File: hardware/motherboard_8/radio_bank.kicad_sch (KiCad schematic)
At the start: 7 parts, among them J1 RADIO 1-4, J2 RADIO 5-8, U2 AMS1117-3.3

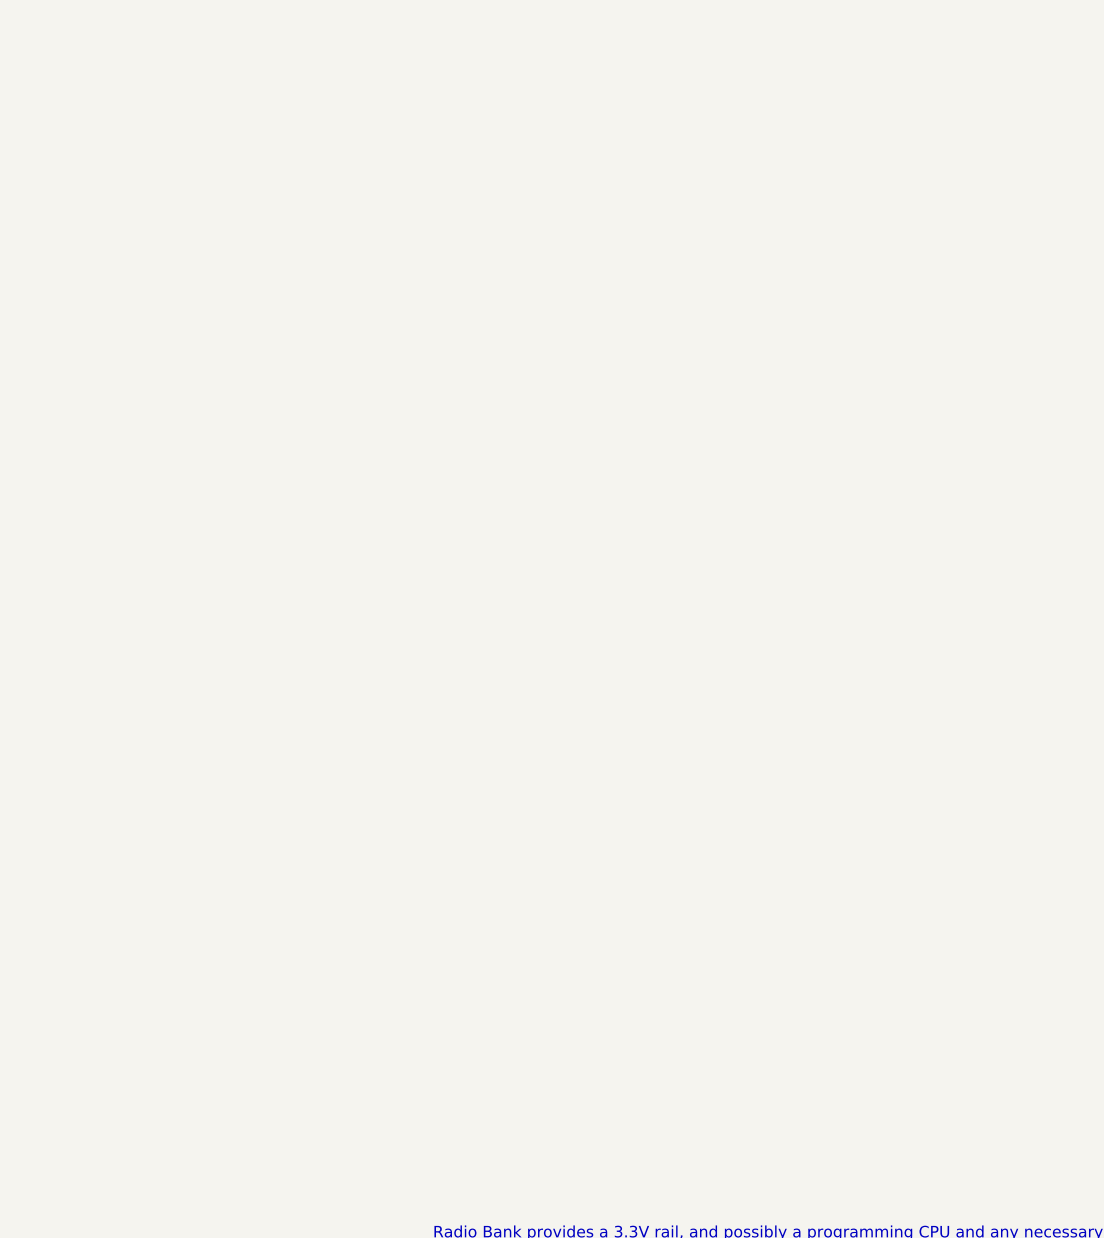
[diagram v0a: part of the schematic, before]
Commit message: Create motherboard 8. Now upgrade number of radios
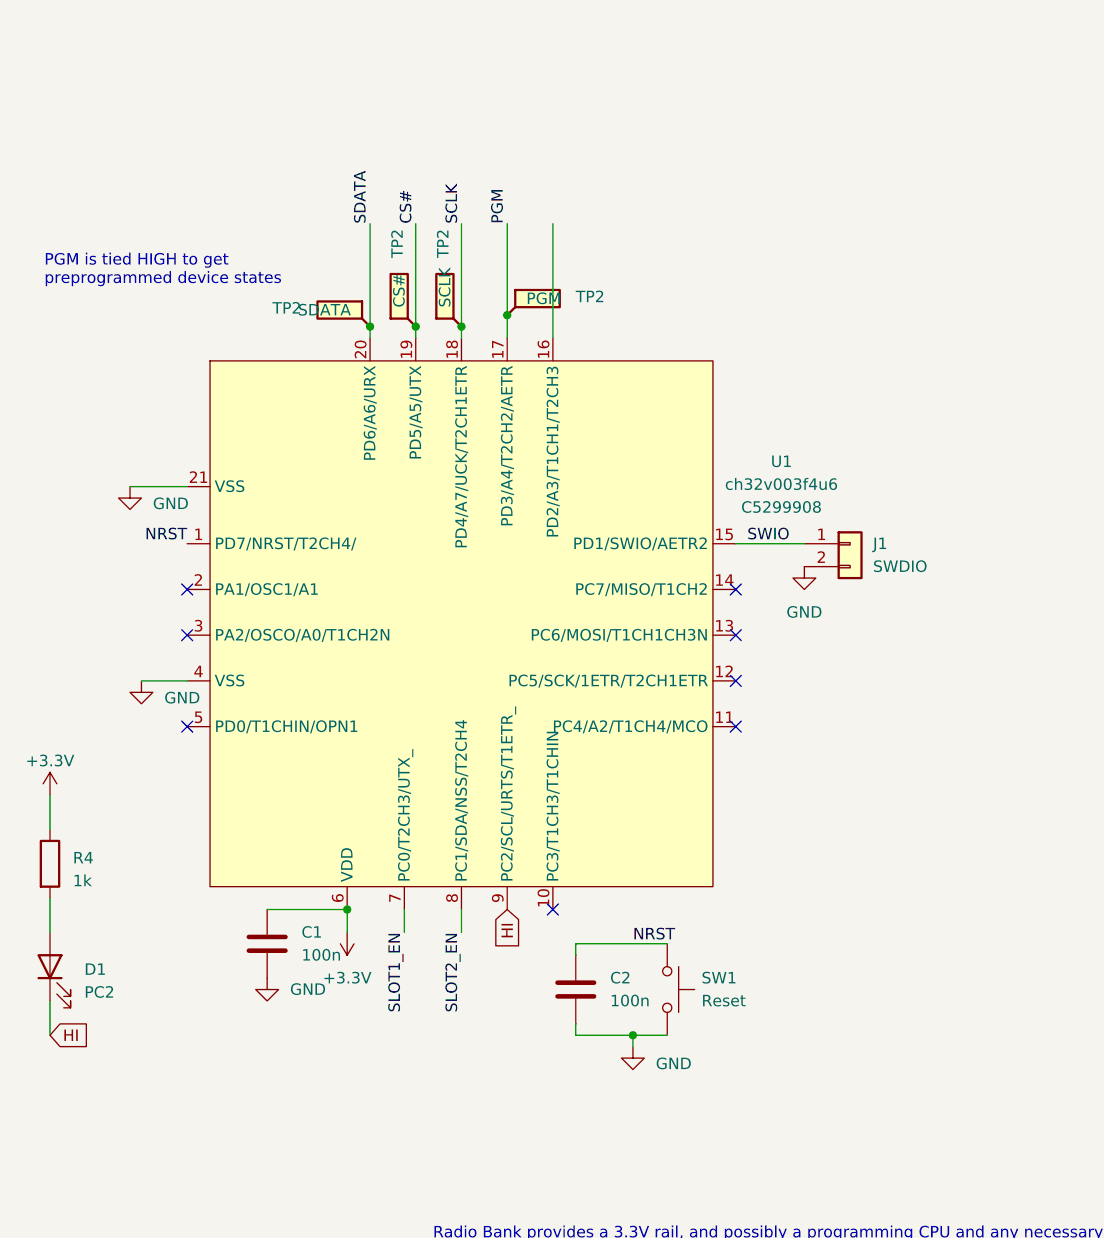
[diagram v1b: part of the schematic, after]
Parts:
- added C1, C2: 100n, Capacitor_SMD:C_0402_1005Metric, symbol Device:C
- added D1: PC2, Diode_SMD:D_0603_1608Metric, symbol Device:LED
- added J1: SWDIO, Connector_JST:JST_PH_B2B-PH-K_1x02_P2.00mm_Vertical, symbol Connector_Generic:Conn_01x02
- added R4: 1k, Resistor_SMD:R_0402_1005Metric, symbol Device:R
- added SW1: Reset, motherboard:TS-1187A-B-A-B, symbol Switch:SW_Push
- added TP2: SCLK, TestPoint:TestPoint_Keystone_5015_Micro-Minature, symbol Connector:TestPoint_Flag
- added TP2: SDATA, TestPoint:TestPoint_Keystone_5015_Micro-Minature, symbol Connector:TestPoint_Flag
- added TP2: CS#, TestPoint:TestPoint_Keystone_5015_Micro-Minature, symbol Connector:TestPoint_Flag
- added TP2: PGM, TestPoint:TestPoint_Keystone_5015_Micro-Minature, symbol Connector:TestPoint_Flag
- added U1: ch32v003f4u6, Package_DFN_QFN:QFN-20-1EP_3x3mm_P0.4mm_EP1.65x1.65mm, symbol ripple:ch32v003f4u6
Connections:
- net CS#: now also TP2.1, U1.19 (PD5/A5/UTX)
- net GND: now also C1.2, C2.2, J1.2 (Pin_2), SW1.2, U1.21 (VSS), U1.4 (VSS)
- net PGM: now also TP2.1, U1.17 (PD3/A4/T2CH2/AETR)
- net SCLK: now also TP2.1, U1.18 (PD4/A7/UCK/T2CH1ETR)
- net SDATA: now also TP2.1, U1.20 (PD6/A6/URX)
- net SLOT1_EN: now also U1.7 (PC0/T2CH3/UTX_)
- net SLOT2_EN: now also U1.8 (PC1/SDA/NSS/T2CH4)
- new net: D1.2 (A), R4.2
- new net +3.3V: C1.1, R4.1, U1.6 (VDD)
- new net HI: D1.1 (K), U1.9 (PC2/SCL/URTS/T1ETR_)
- new net NRST: C2.1, SW1.1, U1.1 (PD7/NRST/T2CH4/)
- new net SWIO: J1.1 (Pin_1), U1.15 (PD1/SWIO/AETR2)
- no-connect marks 0 -> 8
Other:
- note added: "PGM is tied HIGH to get preprogrammed device states"
